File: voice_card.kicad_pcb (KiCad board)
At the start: 2 copper layers, 133.3 x 30 mm, 207 parts, among them J1 PCI_11_49, Q1 MMBF4391LT1G, Q10 DMMT3906, Q11 BC857BS, Q2 2N3904, Q3 BCM847, Q4 DMMT3904, Q5 DMMT3906, Q6 MMBF4391LT1G, Q7 BCM847, Q8 2N3904, Q9 DMMT3904, U1 TL074-, U10 TL072-, U11 TL074-, U12 NE555, U13 LM311M, U14 CD4052, U15 TL072-, U16 TL072-, U17 LM13700, U18 LM13700, U19 LM13700, U2 TL074-, U20 TL072-, U3 NE555, U4 LF351, U5 TL072-, U6 LM311M, U7 CD4052, U8 TL074-, U9 LF351

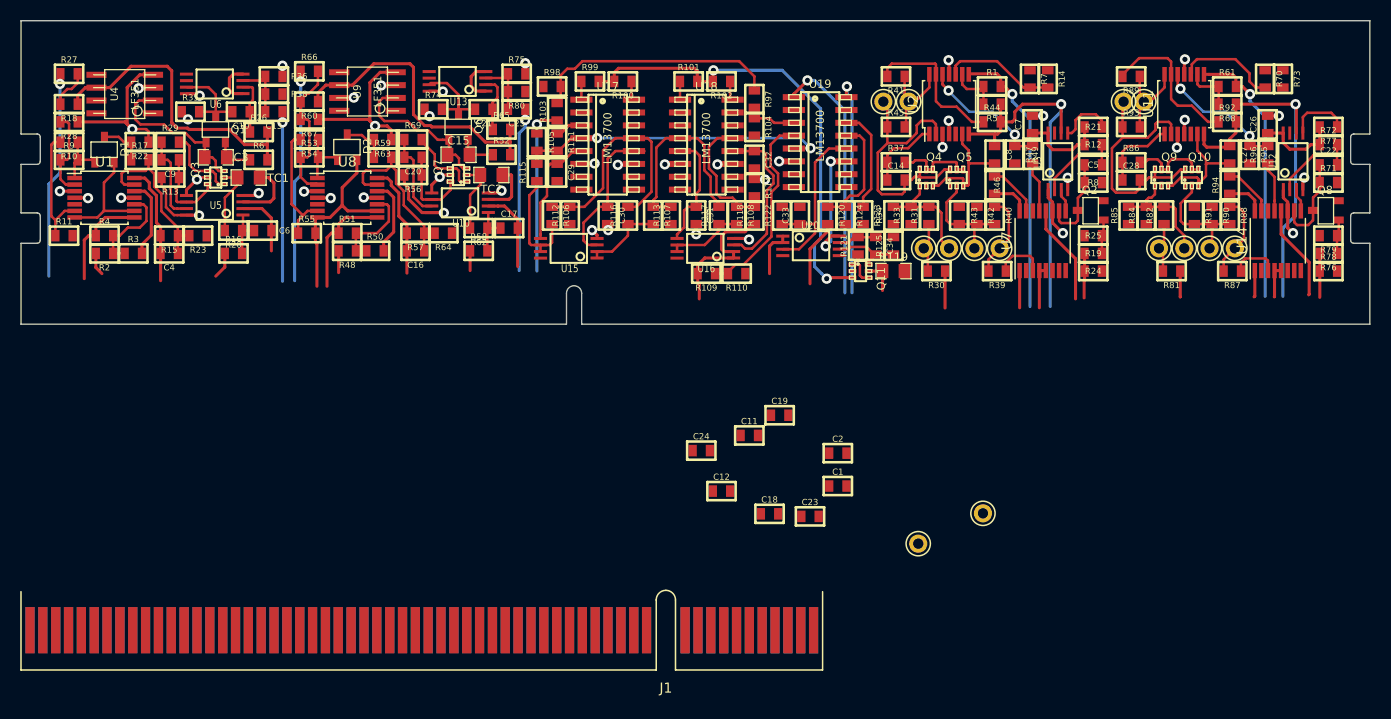
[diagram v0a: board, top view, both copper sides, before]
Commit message: DDR3 DIMM schematic symbol created, now assigning ins and outs to DIMM pins. Tedious
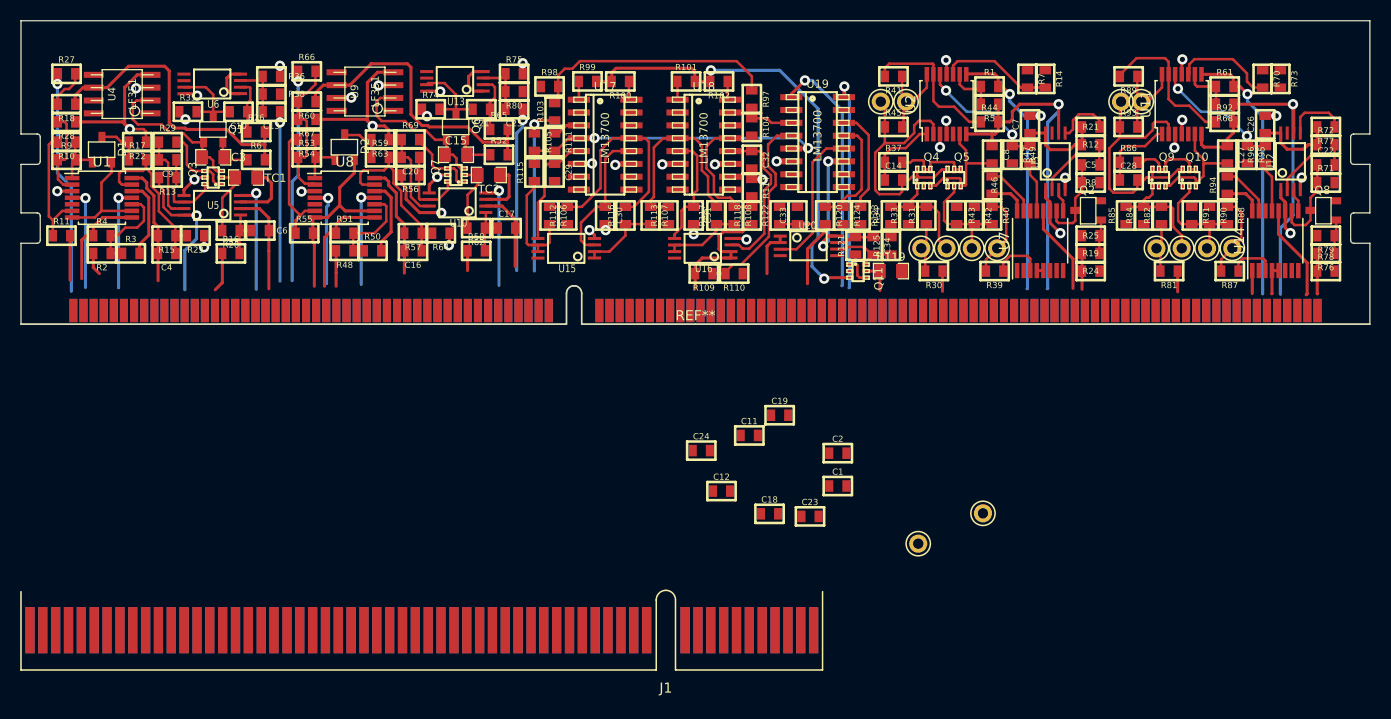
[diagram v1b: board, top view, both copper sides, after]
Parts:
- added REF**: DDR3-DIMM-MO-269, MyModules:DDR3-DIMM-MO-269, F.Cu at (140.2, 89.2)
- moved C10 0.25 mm to (95.0, 69.5)
- moved C13 0.25 mm to (98.2, 69.5)
- moved C14 0.25 mm to (159.8, 76.2)
- moved C15 0.25 mm to (116.5, 73.8)
- moved C16 0.25 mm to (112.2, 83.2)
- moved C17 0.25 mm to (121.5, 81.0)
- moved C20 0.25 mm to (112.0, 74.0)
- moved C21 0.25 mm to (119.0, 69.2)
- moved C22 0.25 mm to (202.5, 74.8)
- moved C25 0.25 mm to (122.2, 69.2)
- moved C26 0.25 mm to (196.5, 70.8)
- moved C27 0.25 mm to (192.8, 73.8)
- moved C28 0.25 mm to (183.0, 76.2)
- moved C29 0.25 mm to (126.2, 75.5)
- moved C3 0.25 mm to (92.5, 74.0)
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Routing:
- net -12V: track 55.9 -> 94.6 mm, vias 13 -> 15
- net +12V: track 67.2 -> 92.4 mm
- net VCO1_SAW: track 11.4 -> 15.8 mm
- net VCO1_PITCH_CV: track 6.44 -> 10.2 mm
- net EG1_RELEASE_CV: track 4.32 -> 0.65 mm
- net EG1_DECAY_CV: track 3.67 -> 0.00 mm
- net EG1_INV_OUT: track 27.4 -> 25.7 mm
- net EG1_ENV_OUT: track 37.6 -> 35.8 mm
- net EG1_ATTACK_CV: track 3.65 -> 2.00 mm
- net VCO1_TRI_SHAPE: track 20.5 -> 22.1 mm
- net VCO2_PWM_CV: track 2.15 -> 3.50 mm
- net VCO1_SCALE: track 2.62 -> 3.89 mm
- net VCF_OUT: track 14.2 -> 13.1 mm
- net EG1_SUSTAIN_CV: track 9.91 -> 8.86 mm
- net EG1_GATE: track 4.42 -> 3.55 mm
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
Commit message: DDR3 DIMM connector switched over from PCI in board and schematic. Routing power traces now
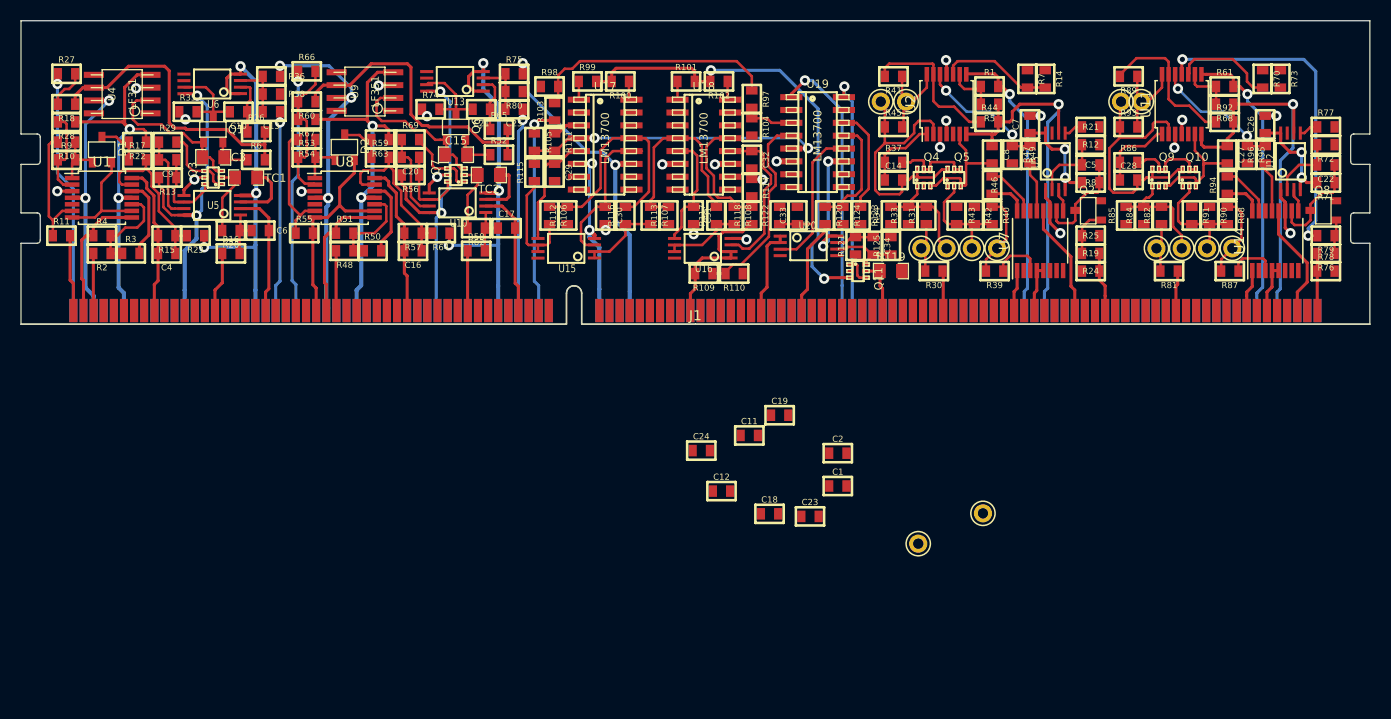
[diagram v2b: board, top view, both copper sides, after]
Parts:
- removed the J1 at (137.2, 120.8)
- J1: renamed from REF**; value DDR3-DIMM-MO-269 -> DDR3-DIMM
- turned C22 to 180 degrees
- turned C5 to 180 degrees
- turned R12 to 180 degrees
- turned R19 to 0 degrees
- turned R21 to 0 degrees
- turned R24 to 180 degrees
- turned R25 to 0 degrees
- turned R71 to 180 degrees
- turned R72 to 180 degrees
- turned R77 to 0 degrees
- turned R8 to 180 degrees
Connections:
- J1 pad 1: (no net) -> VCO1_SAW
- J1 pad 10: (no net) -> Net-(J1-Pad10)
- J1 pad 100: (no net) -> GND
- J1 pad 101: (no net) -> Net-(J1-Pad101)
- J1 pad 102: (no net) -> Net-(J1-Pad102)
- J1 pad 103: (no net) -> Net-(J1-Pad103)
- J1 pad 104: (no net) -> Net-(J1-Pad104)
- J1 pad 105: (no net) -> Net-(J1-Pad105)
- J1 pad 106: (no net) -> EG2_ATTACK_CV
- J1 pad 107: (no net) -> Net-(J1-Pad107)
- J1 pad 108: (no net) -> Net-(J1-Pad108)
- J1 pad 109: (no net) -> Net-(J1-Pad109)
- J1 pad 11: (no net) -> Net-(J1-Pad11)
- J1 pad 110: (no net) -> Net-(J1-Pad110)
- J1 pad 111: (no net) -> Net-(J1-Pad111)
- J1 pad 112: (no net) -> Net-(J1-Pad112)
- J1 pad 113: (no net) -> EG2_DECAY_CV
- J1 pad 114: (no net) -> Net-(J1-Pad114)
- J1 pad 115: (no net) -> EG2_RELEASE_CV
- J1 pad 116: (no net) -> Net-(J1-Pad116)
- J1 pad 117: (no net) -> Net-(J1-Pad117)
- J1 pad 118: (no net) -> EG2_SUSTAIN_CV
- J1 pad 119: (no net) -> Net-(J1-Pad119)
- J1 pad 12: (no net) -> Net-(J1-Pad12)
- J1 pad 120: (no net) -> EG2_GATE
- J1 pad 121: (no net) -> VCO1_TRI_SHAPE
- J1 pad 122: (no net) -> Net-(J1-Pad122)
- J1 pad 123: (no net) -> +12V
- J1 pad 124: (no net) -> GND
- J1 pad 125: (no net) -> GND
- J1 pad 126: (no net) -> -12V
- J1 pad 127: (no net) -> Net-(J1-Pad127)
- J1 pad 128: (no net) -> Net-(J1-Pad128)
- J1 pad 129: (no net) -> Net-(J1-Pad129)
- J1 pad 13: (no net) -> Net-(J1-Pad13)
- J1 pad 130: (no net) -> Net-(J1-Pad130)
- J1 pad 131: (no net) -> Net-(J1-Pad131)
- J1 pad 132: (no net) -> +12V
- J1 pad 133: (no net) -> Net-(J1-Pad133)
- J1 pad 134: (no net) -> Net-(J1-Pad134)
- J1 pad 135: (no net) -> Net-(J1-Pad135)
- J1 pad 136: (no net) -> Net-(J1-Pad136)
- J1 pad 137: (no net) -> Net-(J1-Pad137)
- J1 pad 138: (no net) -> Net-(J1-Pad138)
- J1 pad 139: (no net) -> -12V
- J1 pad 14: (no net) -> Net-(J1-Pad14)
- J1 pad 140: (no net) -> GND
- J1 pad 141: (no net) -> VCO1_SYNC_IN
- J1 pad 142: (no net) -> GND
- J1 pad 143: (no net) -> VCO2_TRI_SHAPE
- J1 pad 144: (no net) -> Net-(J1-Pad144)
- J1 pad 145: (no net) -> Net-(J1-Pad145)
- J1 pad 146: (no net) -> +12V
- J1 pad 147: (no net) -> GND
- J1 pad 148: (no net) -> GND
- J1 pad 149: (no net) -> -12V
- J1 pad 15: (no net) -> VCO1_SCALE
- J1 pad 150: (no net) -> Net-(J1-Pad150)
- J1 pad 151: (no net) -> Net-(J1-Pad151)
- J1 pad 152: (no net) -> Net-(J1-Pad152)
- J1 pad 153: (no net) -> Net-(J1-Pad153)
- J1 pad 154: (no net) -> Net-(J1-Pad154)
- J1 pad 155: (no net) -> Net-(J1-Pad155)
- J1 pad 156: (no net) -> Net-(J1-Pad156)
- J1 pad 157: (no net) -> +12V
- J1 pad 158: (no net) -> Net-(J1-Pad158)
- J1 pad 159: (no net) -> Net-(J1-Pad159)
- J1 pad 16: (no net) -> Net-(J1-Pad16)
- J1 pad 160: (no net) -> Net-(J1-Pad160)
- J1 pad 161: (no net) -> Net-(J1-Pad161)
- J1 pad 162: (no net) -> Net-(J1-Pad162)
- J1 pad 163: (no net) -> -12V
- J1 pad 164: (no net) -> Net-(J1-Pad164)
- J1 pad 165: (no net) -> VCO2_SYNC_IN
- J1 pad 166: (no net) -> GND
- J1 pad 167: (no net) -> VCF_IN
- J1 pad 168: (no net) -> GND
- J1 pad 169: (no net) -> -12V
- J1 pad 17: (no net) -> Net-(J1-Pad17)
- J1 pad 170: (no net) -> Net-(J1-Pad170)
- J1 pad 171: (no net) -> Net-(J1-Pad171)
- J1 pad 172: (no net) -> +12V
- J1 pad 173: (no net) -> Net-(J1-Pad173)
- J1 pad 174: (no net) -> Net-(J1-Pad174)
- J1 pad 175: (no net) -> Net-(J1-Pad175)
- J1 pad 176: (no net) -> Net-(J1-Pad176)
- J1 pad 177: (no net) -> Net-(J1-Pad177)
- J1 pad 178: (no net) -> Net-(J1-Pad178)
- J1 pad 179: (no net) -> Net-(J1-Pad179)
- J1 pad 18: (no net) -> Net-(J1-Pad18)
- J1 pad 180: (no net) -> Net-(J1-Pad180)
- J1 pad 181: (no net) -> Net-(J1-Pad181)
- J1 pad 182: (no net) -> Net-(J1-Pad182)
- J1 pad 183: (no net) -> Net-(J1-Pad183)
- J1 pad 184: (no net) -> Net-(J1-Pad184)
- J1 pad 185: (no net) -> Net-(J1-Pad185)
- J1 pad 186: (no net) -> Net-(J1-Pad186)
- J1 pad 187: (no net) -> Net-(J1-Pad187)
- J1 pad 188: (no net) -> Net-(J1-Pad188)
- J1 pad 189: (no net) -> Net-(J1-Pad189)
- J1 pad 19: (no net) -> Net-(J1-Pad19)
- J1 pad 190: (no net) -> Net-(J1-Pad190)
- J1 pad 191: (no net) -> Net-(J1-Pad191)
- J1 pad 192: (no net) -> Net-(J1-Pad192)
- J1 pad 193: (no net) -> RES_CTRL
- J1 pad 194: (no net) -> VCA_CTRL
- J1 pad 195: (no net) -> Net-(J1-Pad195)
- J1 pad 196: (no net) -> Net-(J1-Pad196)
- J1 pad 197: (no net) -> Net-(J1-Pad197)
- J1 pad 198: (no net) -> Net-(J1-Pad198)
- J1 pad 199: (no net) -> Net-(J1-Pad199)
- J1 pad 2: (no net) -> VCO1_PULSE
- J1 pad 20: (no net) -> VCO1_PITCH_CV
- J1 pad 200: (no net) -> Net-(J1-Pad200)
- J1 pad 201: (no net) -> Net-(J1-Pad201)
- J1 pad 202: (no net) -> Net-(J1-Pad202)
- J1 pad 203: (no net) -> Net-(J1-Pad203)
- J1 pad 204: (no net) -> Net-(J1-Pad204)
- J1 pad 205: (no net) -> Net-(J1-Pad205)
- J1 pad 206: (no net) -> Net-(J1-Pad206)
- J1 pad 207: (no net) -> Net-(J1-Pad207)
- J1 pad 208: (no net) -> Net-(J1-Pad208)
- J1 pad 209: (no net) -> Net-(J1-Pad209)
- J1 pad 21: (no net) -> GND
- J1 pad 210: (no net) -> Net-(J1-Pad210)
- J1 pad 211: (no net) -> EG1_INV_OUT
- J1 pad 212: (no net) -> GND
- J1 pad 213: (no net) -> EG1_ENV_OUT
- J1 pad 214: (no net) -> Net-(J1-Pad214)
- J1 pad 215: (no net) -> Net-(J1-Pad215)
- J1 pad 216: (no net) -> Net-(J1-Pad216)
- J1 pad 217: (no net) -> Net-(J1-Pad217)
- J1 pad 218: (no net) -> Net-(J1-Pad218)
- J1 pad 219: (no net) -> Net-(J1-Pad219)
- J1 pad 22: (no net) -> Net-(J1-Pad22)
- J1 pad 220: (no net) -> Net-(J1-Pad220)
- J1 pad 221: (no net) -> Net-(J1-Pad221)
- J1 pad 222: (no net) -> Net-(J1-Pad222)
- J1 pad 223: (no net) -> Net-(J1-Pad223)
- J1 pad 224: (no net) -> Net-(J1-Pad224)
- J1 pad 225: (no net) -> Net-(J1-Pad225)
- J1 pad 226: (no net) -> Net-(J1-Pad226)
- J1 pad 227: (no net) -> Net-(J1-Pad227)
- J1 pad 228: (no net) -> Net-(J1-Pad228)
- J1 pad 229: (no net) -> Net-(J1-Pad229)
- J1 pad 23: (no net) -> Net-(J1-Pad23)
- J1 pad 230: (no net) -> Net-(J1-Pad230)
- J1 pad 231: (no net) -> Net-(J1-Pad231)
- J1 pad 232: (no net) -> Net-(J1-Pad232)
- J1 pad 233: (no net) -> Net-(J1-Pad233)
- J1 pad 234: (no net) -> EG2_INV_OUT
- J1 pad 235: (no net) -> GND
- J1 pad 236: (no net) -> EG2_ENV_OUT
- J1 pad 237: (no net) -> Net-(J1-Pad237)
- J1 pad 238: (no net) -> Net-(J1-Pad238)
- J1 pad 239: (no net) -> Net-(J1-Pad239)
- J1 pad 24: (no net) -> Net-(J1-Pad24)
- J1 pad 240: (no net) -> Net-(J1-Pad240)
- J1 pad 25: (no net) -> VCO2_SAW
- J1 pad 26: (no net) -> VCO2_PULSE
- J1 pad 27: (no net) -> VCO2_PWM_CV
- J1 pad 28: (no net) -> Net-(J1-Pad28)
- J1 pad 29: (no net) -> Net-(J1-Pad29)
- J1 pad 3: (no net) -> VCO1_PWM_CV
- J1 pad 30: (no net) -> Net-(J1-Pad30)
- J1 pad 31: (no net) -> Net-(J1-Pad31)
- J1 pad 32: (no net) -> Net-(J1-Pad32)
- J1 pad 33: (no net) -> Net-(J1-Pad33)
- J1 pad 34: (no net) -> VCO2_TRI
- J1 pad 35: (no net) -> Net-(J1-Pad35)
- J1 pad 36: (no net) -> Net-(J1-Pad36)
- J1 pad 37: (no net) -> Net-(J1-Pad37)
- J1 pad 38: (no net) -> Net-(J1-Pad38)
- J1 pad 39: (no net) -> Net-(J1-Pad39)
- J1 pad 4: (no net) -> GND
- J1 pad 40: (no net) -> VCO2_SCALE
- J1 pad 41: (no net) -> Net-(J1-Pad41)
- J1 pad 42: (no net) -> Net-(J1-Pad42)
- J1 pad 43: (no net) -> Net-(J1-Pad43)
- J1 pad 44: (no net) -> GND
- J1 pad 45: (no net) -> VCO2_PITCH_CV
- J1 pad 46: (no net) -> GND
- J1 pad 47: (no net) -> Net-(J1-Pad47)
- J1 pad 48: (no net) -> Net-(J1-Pad48)
- J1 pad 49: (no net) -> Net-(J1-Pad49)
- J1 pad 5: (no net) -> GND
- J1 pad 50: (no net) -> Net-(J1-Pad50)
- J1 pad 51: (no net) -> Net-(J1-Pad51)
- J1 pad 52: (no net) -> Net-(J1-Pad52)
- J1 pad 53: (no net) -> Net-(J1-Pad53)
- J1 pad 54: (no net) -> Net-(J1-Pad54)
- J1 pad 55: (no net) -> Net-(J1-Pad55)
- J1 pad 56: (no net) -> Net-(J1-Pad56)
- J1 pad 57: (no net) -> Net-(J1-Pad57)
- J1 pad 58: (no net) -> VCF_OUT
- J1 pad 59: (no net) -> Net-(J1-Pad59)
- J1 pad 6: (no net) -> Net-(J1-Pad6)
- J1 pad 60: (no net) -> Net-(J1-Pad60)
- J1 pad 61: (no net) -> Net-(J1-Pad61)
- J1 pad 62: (no net) -> Net-(J1-Pad62)
- J1 pad 63: (no net) -> Net-(J1-Pad63)
- J1 pad 64: (no net) -> Net-(J1-Pad64)
- J1 pad 65: (no net) -> VCA_OUT
- J1 pad 66: (no net) -> Net-(J1-Pad66)
- J1 pad 67: (no net) -> Net-(J1-Pad67)
- J1 pad 68: (no net) -> Net-(J1-Pad68)
- J1 pad 69: (no net) -> VCA_IN
- J1 pad 7: (no net) -> Net-(J1-Pad7)
- J1 pad 70: (no net) -> Net-(J1-Pad70)
- J1 pad 71: (no net) -> Net-(J1-Pad71)
- J1 pad 72: (no net) -> Net-(J1-Pad72)
- J1 pad 73: (no net) -> Net-(J1-Pad73)
- J1 pad 74: (no net) -> Net-(J1-Pad74)
- J1 pad 75: (no net) -> Net-(J1-Pad75)
- J1 pad 76: (no net) -> Net-(J1-Pad76)
- J1 pad 77: (no net) -> VCF_CTRL
- J1 pad 78: (no net) -> Net-(J1-Pad78)
- J1 pad 79: (no net) -> Net-(J1-Pad79)
- J1 pad 8: (no net) -> Net-(J1-Pad8)
- J1 pad 80: (no net) -> Net-(J1-Pad80)
- J1 pad 81: (no net) -> Net-(J1-Pad81)
- J1 pad 82: (no net) -> Net-(J1-Pad82)
- J1 pad 83: (no net) -> EG1_ATTACK_CV
- J1 pad 84: (no net) -> Net-(J1-Pad84)
- J1 pad 85: (no net) -> Net-(J1-Pad85)
- J1 pad 86: (no net) -> Net-(J1-Pad86)
- J1 pad 87: (no net) -> Net-(J1-Pad87)
- J1 pad 88: (no net) -> Net-(J1-Pad88)
- J1 pad 89: (no net) -> Net-(J1-Pad89)
- J1 pad 9: (no net) -> VCO1_TRI
- J1 pad 90: (no net) -> EG1_DECAY_CV
- J1 pad 91: (no net) -> Net-(J1-Pad91)
- J1 pad 92: (no net) -> EG1_RELEASE_CV
- J1 pad 93: (no net) -> Net-(J1-Pad93)
- J1 pad 94: (no net) -> Net-(J1-Pad94)
- J1 pad 95: (no net) -> Net-(J1-Pad95)
- J1 pad 96: (no net) -> EG1_SUSTAIN_CV
- J1 pad 97: (no net) -> GND
- J1 pad 98: (no net) -> Net-(J1-Pad98)
- J1 pad 99: (no net) -> EG1_GATE
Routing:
- net -12V: track 94.6 -> 203.8 mm, vias 15 -> 18
- net +12V: track 92.4 -> 198.8 mm, vias 17 -> 20
- net VCO2_PITCH_CV: track 8.12 -> 12.6 mm
- net Net-(R77-Pad1): track 6.20 -> 1.93 mm
- net VCF_IN: track 17.6 -> 21.6 mm
- net EG1_DECAY_CV: track 0.00 -> 4.07 mm
- net EG1_RELEASE_CV: track 0.65 -> 4.70 mm
- net VCO2_SCALE: track 1.95 -> 5.91 mm
- net VCA_OUT: track 4.81 -> 8.69 mm
- net VCO2_SYNC_IN: track 16.2 -> 20.1 mm
- net VCO2_TRI: track 11.2 -> 15.0 mm
- net Net-(R21-Pad1): track 5.57 -> 1.93 mm
- net VCO1_PWM_CV: track 2.25 -> 5.66 mm
- net VCO1_PULSE: track 10.2 -> 13.4 mm
- net VCO1_SAW: track 15.8 -> 18.9 mm
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
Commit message: power routed, now stitching grounds
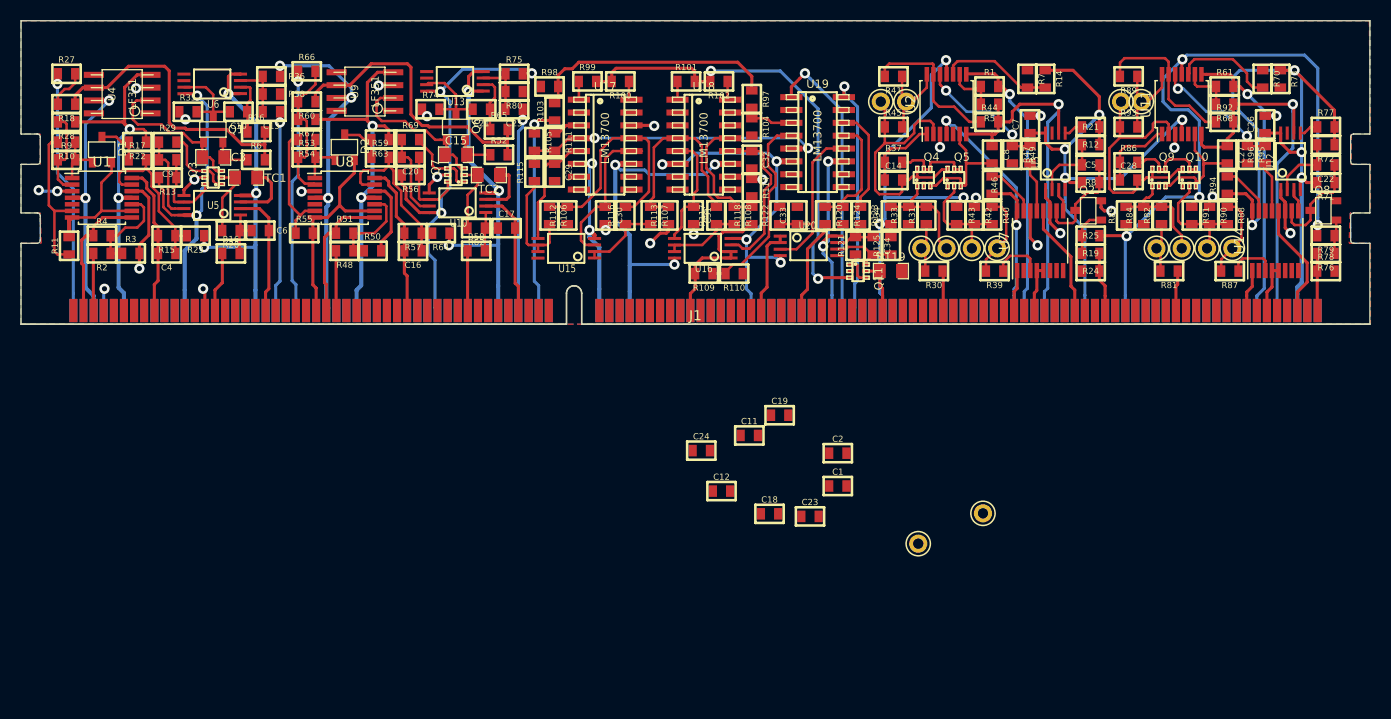
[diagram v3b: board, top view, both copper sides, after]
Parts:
- moved R11 1.25 mm to (78.2, 82.8), turned to 90 degrees
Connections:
- J1 pad 114: Net-(J1-Pad114) -> GND
- J1 pad 116: Net-(J1-Pad116) -> GND
- J1 pad 117: Net-(J1-Pad117) -> GND
- J1 pad 119: Net-(J1-Pad119) -> GND
- J1 pad 12: Net-(J1-Pad12) -> GND
- J1 pad 127: Net-(J1-Pad127) -> GND
- J1 pad 128: Net-(J1-Pad128) -> GND
- J1 pad 129: Net-(J1-Pad129) -> GND
- J1 pad 135: Net-(J1-Pad135) -> GND
- J1 pad 14: Net-(J1-Pad14) -> GND
- J1 pad 160: Net-(J1-Pad160) -> GND
- J1 pad 177: Net-(J1-Pad177) -> GND
- J1 pad 178: Net-(J1-Pad178) -> GND
- J1 pad 179: Net-(J1-Pad179) -> GND
- J1 pad 184: Net-(J1-Pad184) -> -12V
- J1 pad 187: Net-(J1-Pad187) -> GND
- J1 pad 188: Net-(J1-Pad188) -> GND
- J1 pad 192: Net-(J1-Pad192) -> +12V
- J1 pad 195: Net-(J1-Pad195) -> GND
- J1 pad 197: Net-(J1-Pad197) -> -12V
- J1 pad 203: Net-(J1-Pad203) -> GND
- J1 pad 204: Net-(J1-Pad204) -> GND
- J1 pad 210: Net-(J1-Pad210) -> +12V
- J1 pad 217: Net-(J1-Pad217) -> +12V
- J1 pad 221: Net-(J1-Pad221) -> -12V
- J1 pad 228: Net-(J1-Pad228) -> GND
- J1 pad 229: Net-(J1-Pad229) -> GND
- J1 pad 238: Net-(J1-Pad238) -> +12V
- J1 pad 239: Net-(J1-Pad239) -> GND
- J1 pad 240: Net-(J1-Pad240) -> GND
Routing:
- net +12V: track 198.8 -> 340.4 mm, vias 20 -> 25
- net -12V: track 203.8 -> 307.5 mm, vias 18 -> 23
- net GND: track 62.2 -> 82.9 mm, vias 17 -> 27
- net VCO1_SAW: track 18.9 -> 13.4 mm
- net Net-(R10-Pad2): track 12.6 -> 15.3 mm
- net RES_CTRL: track 26.9 -> 27.9 mm
- net Net-(R89-Pad2): track 15.1 -> 15.8 mm
- added copper zone on B.Cu, net GND
- added copper zone on F.Cu, net GND

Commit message: stitching ground plane
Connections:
- J1 pad 102: Net-(J1-Pad102) -> GND
- J1 pad 103: Net-(J1-Pad103) -> GND
- J1 pad 151: Net-(J1-Pad151) -> GND
- J1 pad 152: Net-(J1-Pad152) -> GND
- J1 pad 219: Net-(J1-Pad219) -> GND
- J1 pad 52: Net-(J1-Pad52) -> GND
- J1 pad 53: Net-(J1-Pad53) -> GND
- J1 pad 59: Net-(J1-Pad59) -> GND
- J1 pad 66: Net-(J1-Pad66) -> GND
- J1 pad 70: Net-(J1-Pad70) -> GND
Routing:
- net GND: track 82.9 -> 99.0 mm, vias 27 -> 31
- net -12V: track 307.5 -> 308.0 mm
